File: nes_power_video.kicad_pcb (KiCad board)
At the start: 2 copper layers, 59.9 x 59.7 mm, 23 parts, among them J2 Audio, J3 Video, J4 Conn_01x05, J5 RGB conn feed, Q1 2SA733, U1 TPS2553DBV

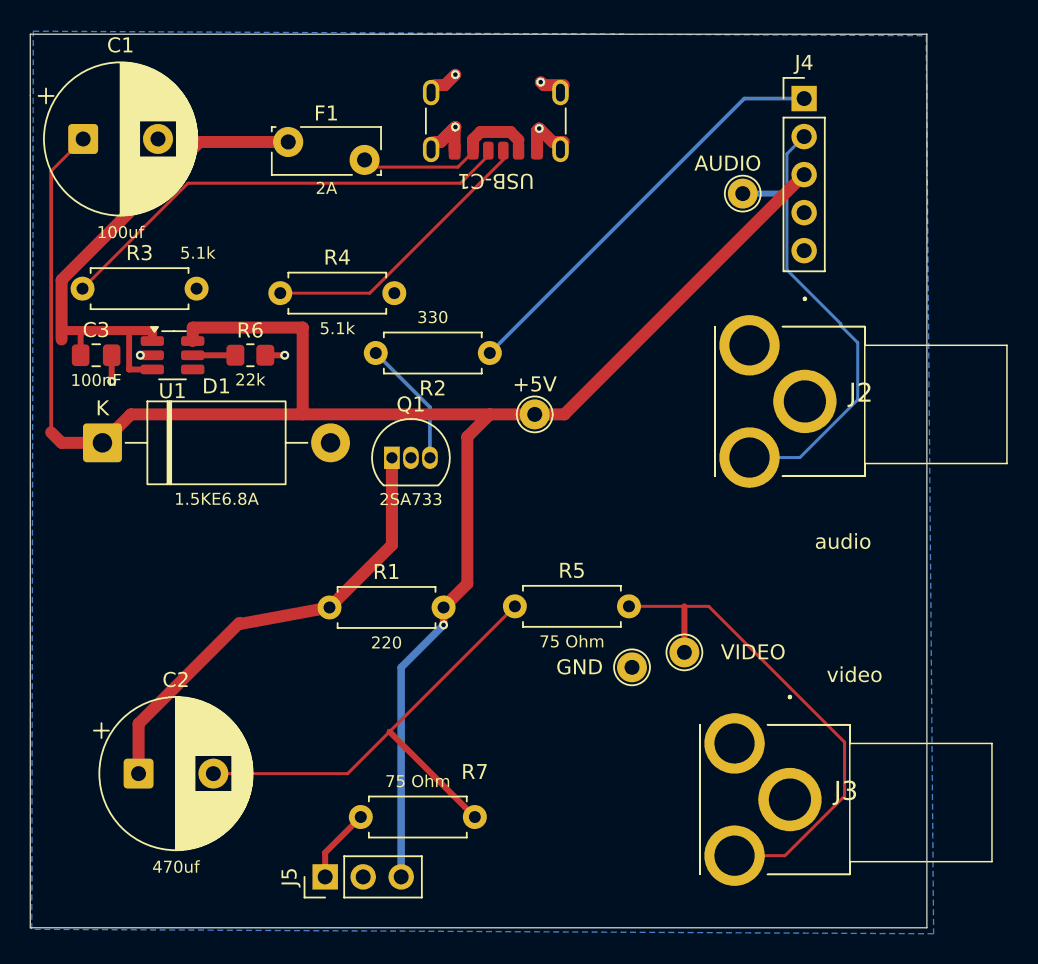
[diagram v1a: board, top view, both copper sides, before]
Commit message: fix(pcb): reroute /raw_5v out of the 0.2mm bottleneck past USB-C1
The VBUS input from USB-C1 to F1 previously ran 7.9mm at 0.2mm track width
through a corridor between USB-C1's ground pads and an adjacent CC2 track -
undersized for F1's 2A hold / 3.8A trip rating on 1oz copper.

Fix has two parts:

- Tightened the Power netclass clearance 0.2mm -> 0.15mm, which opened just
  enough margin in that corridor to route the full path at 0.8mm, with only
  two short (0.68mm, 0.71mm) 0.2mm neck-downs directly at the pads where no
  more room exists. Total narrow-gauge length dropped from 7.9mm to 1.47mm,
  and it's now sandwiched between wide copper rather than in series across
  the whole span.

- The tighter clearance also broke the ground pour's thermal-relief spoke
  count at J2 pin 1 (GND) down to 1 (min 2 required) - J2 pin 3 (unused
  SHUNT) sits close enough that its isolation gap was eating the remaining
  spoke direction. Rather than fight the geometry, set pad 1's zone
  connection to Solid instead of thermal relief: it's a through-hole jack,
  hand-soldered, so the extra thermal mass isn't a soldering concern the way
  it would be on SMD/reflow parts.

Verified: DRC 0 errors / 0 unconnected / schematic parity clean, check_nets.py
invariants hold, and /raw_5v forms a single connected copper path from F1
through to both USB-C1 VBUS pads (A9, B9).

Co-Authored-By: Claude Sonnet 5 <noreply@anthropic.com>
Claude-Session: https://claude.ai/code/session_01WYRpQwnwUmWdzqXMnPsmkw
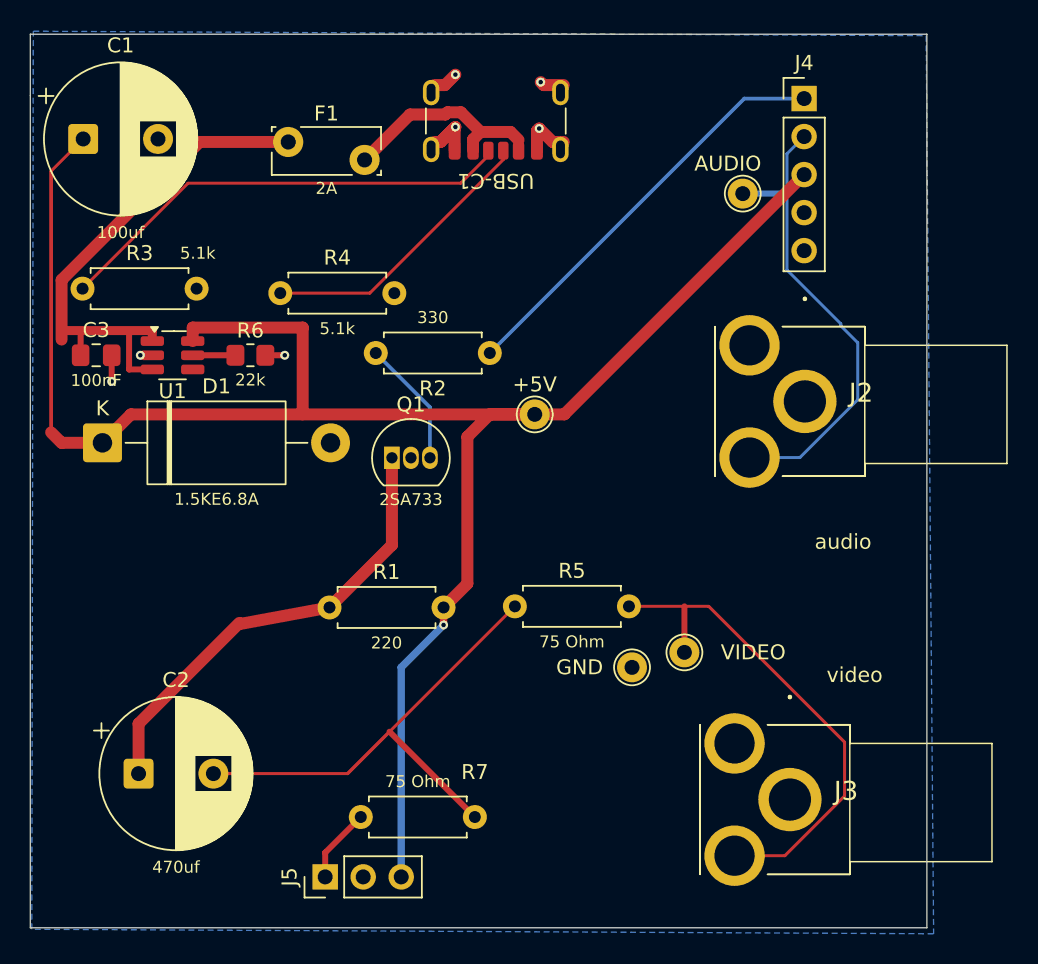
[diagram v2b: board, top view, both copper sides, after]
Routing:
- net /VIDEO_BUF: track 32.8 -> 36.8 mm
- net /5V: track 143.7 -> 146.7 mm
- net /raw_5v: track 12.9 -> 15.3 mm

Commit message: sourcing(v2): move USB-C1, F1 and D1 to LCSC parts
Closes the last non-LCSC lines on the v2 BOM so the whole SMD assembly
BOM can be sourced from one place, which is what U1's Western stockout
forced in the first place.

USB-C1: GCT USB4970-00-A -> USB4125-GF-A-0190 (LCSC C5246813).
LCSC does not stock the USB4970 at all, so searching that MPN was always
going to come up empty. The USB4125 is a different GCT line number that
LCSC does carry, and the board was already laid out to its land pattern
-- the KiCad footprints for USB4125-xx-x and USB4125-xx-x-0190 are
byte-identical in copper, silk, fab, courtyard and drills, differing only
in name, descr and 3D model. Verified against GCT's own drawing: pad
centres 1.00/3.04/5.50 mm, shell holes 8.64 x 3.80 mm, and the ordering
table's "Blank = 1.00mm, 0190 = 1.90mm" stake codes. The -0190 is chosen
because its 1.90 mm stake protrudes 0.30 mm through this 1.6 mm board and
gives a bottom-side fillet, where the 1.00 mm stake does not reach through.
No layout change: zero copper or geometry lines differ.

F1: Littelfuse RHEF200 -> Jinrui JK30-200 (LCSC C369104).
LCSC does not stock the RHEF series. IH 2.0 A unchanged, IT 3.8 -> 4.0 A,
resistance improves slightly (40/100 mOhm vs 45/110), 30 V rather than
16 V, Imax 100 -> 40 A. Confirmed radial leaded from the JK30 datasheet:
D(typ) lead spacing 5.1 mm, tinned 24AWG/0.5 mm leads, C(max) 3.0 mm body
thickness, all consistent with the Bourns MF-RG300 land pattern F1 borrows.

The JKSEMI JK16-200T (C5183874) was evaluated first and rejected: LCSC
lists it as Through Hole P=5.1mm, but its own datasheet is headed "JK16
Series Surface Mount PTC Devices" and LCSC has no land pattern drawn for
it. The package could not be confirmed, so it is called out as a
do-not-substitute in both BOM.csv and the README.

D1: LCSC C294199 added as a second source. That stock is DOWO-branded
(VWM 5.8 V, VBR 6.46 V, VC 10.5 V @ 142.86 A), equivalent to the
Littelfuse figures the design was character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
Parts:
- USB-C1: value USB4970-00-A -> USB4125-GF-A-0190; footprint Connector_USB:USB_C_Receptacle_GCT_USB4125-xx-x_6P_TopMnt_Horizontal -> Connector_USB:USB_C_Receptacle_GCT_USB4125-xx-x-0190_6P_TopMnt_Horizontal
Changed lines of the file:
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@@
 			)
 		)
-		(property "Datasheet" "https://www.littelfuse.com/assetdocs/resettable-ptc-rhef-datasheet?assetguid=5c5a29fe-1611-4d65-b4ce-dc979c44d206"
+		(property "Datasheet" "https://www.lcsc.com/datasheet/C369104.pdf"
 			(at 0 0 0)
 			(layer "F.Fab")
@@
 			)
 		)
-		(property "Manufacturer" "Littelfuse"
+		(property "Manufacturer" "Jinrui (ShenZhen JinRui Electronic Material)"
+			(at 0 0 0)
+			(layer "F.Fab")
+			(hide yes)
+			(effects
+				(font
+					(size 1.27 1.27)
+					(thickness 0.15)
+				)
+			)
+		)
+		(property "MPN" "JK30-200"
 			(at 0 0 0)
 			(layer "F.Fab")
@@
 			)
 		)
-		(property "MPN" "RHEF200"
+		(property "BOM Comments" "Replaces Littelfuse RHEF200, which LCSC does not stock. IH 2.0 A unchanged; IT rises 3.8 A -> 4.0 A; resistance improves slightly (Rmin 40 / R1max 100 mOhm vs the RHEF200's 45/110), so marginally less drop on the 5 V rail. Imax drops 100 A -> 40 A: that is the maximum fault current the device can interrupt, and a USB-C source limited to ~3 A never approaches it. CHECK HEIGHT BEFORE ORDERING: B(max) is 15.2 mm against the RHEF200's ~9-10 mm, and radial PPTCs stand vertically, so this is ~5-6 mm more height above the board inside the NES shell. F1 sits 7.2 mm from the top board edge. Sourcing checked 2026-09-09: 5,800 in stock, MOQ 10, multiple 10, $0.063 at qty 10. NOT the JKSEMI JK16-200T (C5183874): LCSC lists that part as Through Hole P=5.1mm, but its own datasheet is headed 'JK16 Series Surface Mount PTC Devices' and LCSC has no land pattern drawn for it, so its package could not be confirmed - do not substitute it without checking the mechanical drawing."
 			(at 0 0 0)
 			(layer "F.Fab")
@@
 			)
 		)
-		(property "Supplier Link" "https://www.digikey.com/en/products/detail/littelfuse-inc/RHEF200/5130265"
+		(property "Supplier Link" "https://www.lcsc.com/product-detail/C369104.html"
 			(at 0 0 0)
 			(layer "F.Fab")
@@
 			)
 		)
-		(property "Spec" "PPTC radial, IH 2.0 A / IT 3.8 A / 16 V max"
+		(property "LCSC" "C369104"
 			(at 0 0 0)
 			(layer "F.Fab")
@@
 			)
 		)
-		(property "Footprint Note" "No Littelfuse RHEF footprint exists in the KiCad libraries. F1 uses the Bourns MF-RG300 land pattern: pads at (0,0) and (5.1,1.2), 5.24 mm centre-to-centre, 1.01 mm drills. RHEF200 leads are 0.51 mm dia at 5.05 +/-0.75 mm spacing, so they fit, but the Bourns part is a 3.0 A/5.1 A device and the drawn body outline is its, not the RHEF200's - do not trust the outline for clearance."
+		(property "Spec" "PPTC radial leaded, IH 2.0 A / IT 4.0 A / 30 V max / Imax 40 A, Rmin 40 mOhm, R1max 100 mOhm, trip 11 s max, 5.1 mm lead pitch, 0.5 mm (24AWG) leads, 3.0 mm body thickness, 15.2 mm max height"
+			(at 0 0 0)
+			(layer "F.Fab")
+			(hide yes)
+			(effects
+				(font
+					(size 1.27 1.27)
+					(thickness 0.15)
+				)
+			)
+		)
+		(property "Footprint Note" "No JK30 footprint exists in the KiCad libraries. F1 uses the Bourns MF-RG300 land pattern: pads at (0,0) and (5.1,1.2), 5.24 mm centre-to-centre, 1.01 mm drills. Confirmed against the JK30 datasheet: the series is radial leaded, D(typ) lead spacing is 5.1 mm and leads are tinned 24AWG / 0.5 mm dia across the whole family, so they seat in the 1.01 mm drills with the same slight splay onto the diagonal pad pair that the RHEF200 needed. C(max) body thickness is 3.0 mm, matching the footprint's 3.0 mm in-plane depth. The silkscreen outline is still the Bourns 3.0 A/5.1 A body, not this part's - do not use it for clearance."
 			(at 0 0 0)
 			(layer "F.Fab")
@@
 		)
 	)
-	(footprint "Connector_USB:USB_C_Receptacle_GCT_USB4125-xx-x_6P_TopMnt_Horizontal"
+	(footprint "Connector_USB:USB_C_Receptacle_GCT_USB4125-xx-x-0190_6P_TopMnt_Horizontal"
 		(layer "F.Cu")
 		(at 49.4 22.4 180)
-		(descr "USB Type C Receptacle, GCT, power-only, 6P, top mounted, horizontal, 3A, 1mm stake: https://gct.co/files/drawings/usb4125.pdf")
+		(descr "USB Type C Receptacle, GCT, power-only, 6P, top mounted, horizontal, 3A, 1.9mm stake: https://gct.co/files/drawings/usb4125.pdf")
 		(tags "USB C Type-C receptacle power-only charging-only 6P 6C right angled")
 		(property "Reference" "USB-C1"
@@
 			)
 		)
-		(property "Value" "USB4970-00-A"
+		(property "Value" "USB4125-GF-A-0190"
 			(at 0 4.725 180)
 			(unlocked yes)
@@
 			)
 		)
-		(property "Datasheet" "https://gct.co/files/drawings/usb4970.pdf"
+		(property "Datasheet" "https://gct.co/files/drawings/usb4125.pdf"
 			(at 0 0 180)
 			(unlocked yes)
@@
 			)
 		)
-		(property "Manufacturer" "GCT"
+		(property "Manufacturer" "Global Connector Technology (GCT)"
+			(at 0 0 0)
+			(layer "F.Fab")
+			(hide yes)
+			(effects
+				(font
+					(size 1.27 1.27)
+					(thickness 0.15)
+				)
+			)
+		)
+		(property "MPN" "USB4125-GF-A-0190"
 			(at 0 0 0)
 			(layer "F.Fab")
@@
 			)
 		)
-		(property "MPN" "USB4970-00-A"
+		(property "BOM Comments" "Replaces GCT USB4970-00-A, which LCSC does not stock - an MPN search will always come up empty. The USB4125 is a different GCT line number that LCSC does carry, and the board was already laid out to its land pattern. Stock is thin (~600-3,700 depending on source) next to the generic Chinese 6P parts, so order spares. Plain 1.00 mm stake variant is C3151650 if the -0190 is out."
 			(at 0 0 0)
 			(layer "F.Fab")
@@
 			)
 		)
-		(property "Supplier Link" "https://www.digikey.com/en/products/detail/gct/USB4970-00-A/28722813"
+		(property "Supplier Link" "https://www.lcsc.com/product-detail/C5246813.html"
 			(at 0 0 0)
 			(layer "F.Fab")
@@
 			)
 		)
-		(property "Spec" "USB Type-C receptacle, 6P power-only (VBUS x2, GND x2, CC1, CC2)"
+		(property "LCSC" "C5246813"
 			(at 0 0 0)
 			(layer "F.Fab")
@@
 			)
 		)
-		(property "Footprint Note" "KiCad has no USB4970 footprint. GCT's USB4970 drawing specifies the same recommended layout as the USB4125: pad centres 1.00/3.04/5.50 mm, widths 0.70/0.76/0.80 mm x 1.20 mm, shell holes 8.64 x 3.80 mm apart, 1.10 x 1.70 mm with 0.60 x 1.20 mm slots. Verified against the drawing 2026-08-28. USB4970-00-A takes the 1.00 mm shell stake, so the plain USB4125-xx-x footprint is the match; -0190 is the 1.90 mm stake variant."
+		(property "Spec" "USB Type-C receptacle, 6P power-only (VBUS x2, GND x2, CC1, CC2), 48 V / 3 A, 20,000 mating cycles, 1.90 mm shell stake"
+			(at 0 0 0)
+			(layer "F.Fab")
+			(hide yes)
+			(effects
+				(font
+					(size 1.27 1.27)
+					(thickness 0.15)
+				)
+			)
+		)
+		(property "Footprint Note" "Exact KiCad footprint for this MPN. USB_C_Receptacle_GCT_USB4125-xx-x-0190 is byte-identical in copper, silk, fab, courtyard and drills to the plain USB4125-xx-x land pattern the board was laid out with - only the name, descr and 3D model differ - so this is a naming correction, not a layout change. The -0190 suffix is the 1.90 mm shell stake, which protrudes 0.30 mm through a 1.6 mm board and gives a bottom-side fillet; the 1.00 mm stake (plain USB4125-GF-A, LCSC C3151650) does not reach through."
 			(at 0 0 0)
 			(layer "F.Fab")
@@
 		)
 		(embedded_fonts no)
-		(model "${KICAD10_3DMODEL_DIR}/Connector_USB.3dshapes/USB_C_Receptacle_GCT_USB4125-xx-x_6P_TopMnt_Horizontal.step"
+		(model "${KICAD10_3DMODEL_DIR}/Connector_USB.3dshapes/USB_C_Receptacle_GCT_USB4125-xx-x-0190_6P_TopMnt_Horizontal.step"
 			(offset
 				(xyz 0 0 0)
@@
 			)
 		)
+		(property "BOM Comments" "LCSC stock of the 1.5KE6.8A is DOWO-branded (C294199, DO-201, MOQ 5): VWM 5.8 V, VBR 6.46 V, VC 10.5 V @ 142.86 A - equivalent to the Littelfuse figures this design was characterised against, so every conclusion in the README still holds, including the finding that D1 does not protect U1. Manufacturer/MPN fields still name Littelfuse because that is the part actually fitted on v1 and the one the DigiKey supplier link points at; 1.5KE6.8A is a generic type number, not a Littelfuse-only MPN. Order either."
+			(at 0 0 0)
+			(layer "F.Fab")
+			(hide yes)
+			(effects
+				(font
+					(size 1.27 1.27)
+					(thickness 0.15)
+				)
+			)
+		)
 		(property "Supplier Link" "https://www.digikey.com/en/products/detail/littelfuse-inc/1-5KE6-8A/285842"
 			(at 0 0 0)
 			(layer "F.Fab")
+			(hide yes)
+			(effects
+				(font
+					(size 1.27 1.27)
+					(thickness 0.15)
+				)
+			)
+		)
+		(property "LCSC" "C294199"
+			(at 0 0 0)
+			(layer "F.Fab")

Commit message: fix(pcb): silence logo parity, drop a duplicate /5V track, add review config
Three unrelated cleanups that all surfaced from one prefab-gate run.

The two silkscreen logos (Mascot_Link_To_Video, OSHW_US002842_Stacked)
had no schematic symbol, so KiCad's parity check reported them as
"Extra footprint" and prefab-gate blocked on it. They are board
graphics, not parts: adding board_only ("Not in schematic") is how
KiCad's own stock LayerMarker_* footprints handle this. Applied to
both placed instances and to all three library footprints so
re-placing one does not reintroduce the finding.

/5V carried a duplicate track: 584a3ce2 ran (19.69,26.8423) ->
(19.69,44.4547) laid directly over 47a13880 plus a 0.15mm tail
(b59aabea) that existed only to meet it. Same-net overlap is invisible
to DRC, which is how it survived. Removing both leaves the real path
(C1 -> D1 pad -> trunk, 20.49mm at 0.2mm) untouched and drops /5V from
38.25mm to 20.49mm of 0.2mm copper. This matters before any rewiden:
widening with the duplicate in place would have left a 0.2mm ghost
underneath at the same coordinates.

.kicad-happy.json records why seven analyzer findings are not defects
-- the 2-layer plane-gap heuristic, filtering on a power-only USB
receptacle and a 75-ohm video output, edge-mounted RCA courtyards, and
the deliberate placement of protection downstream of the connector.
EMC risk score 67 -> 97.

Verified: DRC --schematic-parity --refill-zones reports 0 errors,
0 unconnected, 0 parity issues (6 pre-existing silkscreen warnings on
J2/J3 remain); tools/check_nets.py passes all invariants with all 14
nets identical between schematic and PCB.

Co-Authored-By: Claude Opus 5 <noreply@anthropic.com>
Claude-Session: https://claude.ai/code/session_01TQL5dscMjqktyVUuQL7XXJ
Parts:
- added #G1: Mascot_Link_To_Video, nes1:Mascot_Link_To_Video, B.Cu at (27.5, 56.0)
- added #G2: OSHW_US002842_Stacked, nes1:OSHW_US002842_Stacked, B.Cu at (56.5, 68.0)
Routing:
- net /5V: track 146.7 -> 128.9 mm
